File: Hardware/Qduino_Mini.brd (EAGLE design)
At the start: 20.3 x 38.1 mm, 40 parts, among them J1 LiPo, Q1 PFET, U1 ATMEGA32U41:1-LESS_PASTE, U2 MCP73831, U3 MAX17048, U4 AP2112K-3.3TRG-1, U5 MIGHTYQ-L-SILK, Y1 8MHZ

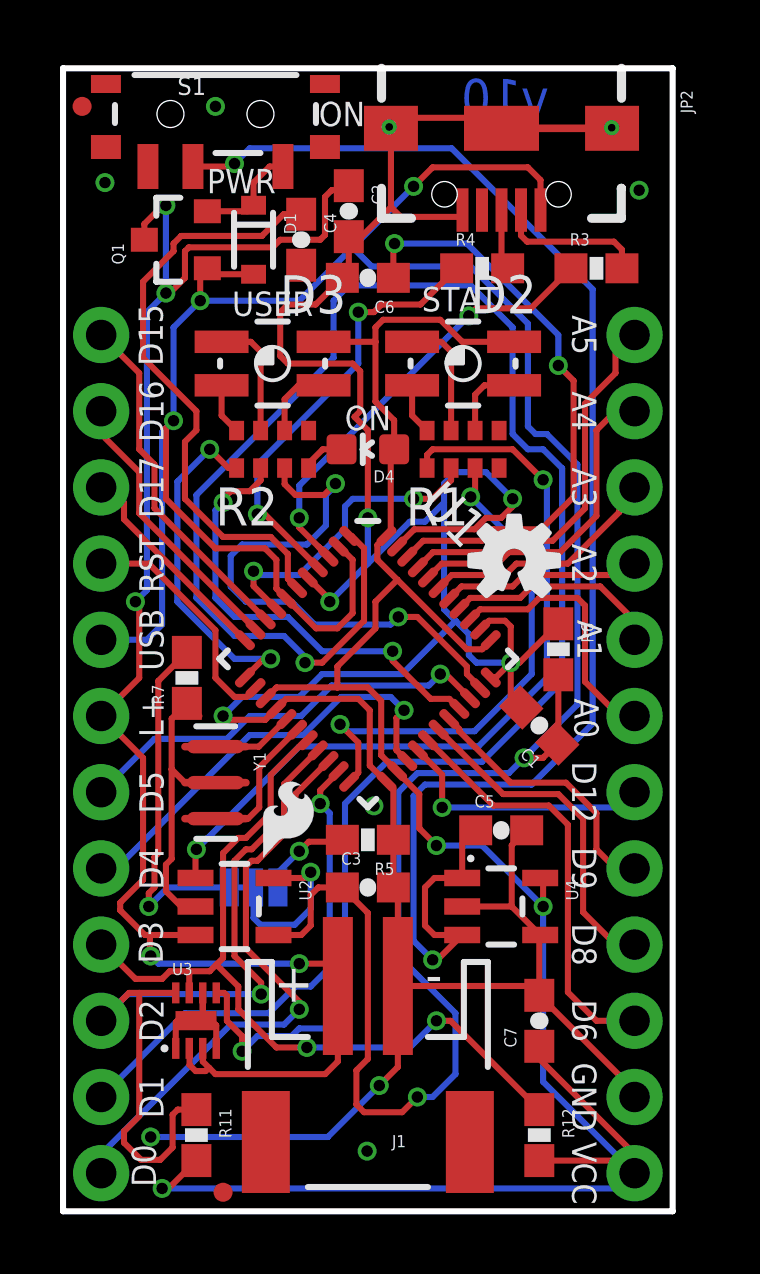
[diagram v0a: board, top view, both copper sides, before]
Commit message: Improved ground path from LiPo to GND pin nearby. Increased width of LiPo & Vbus by 25-50%
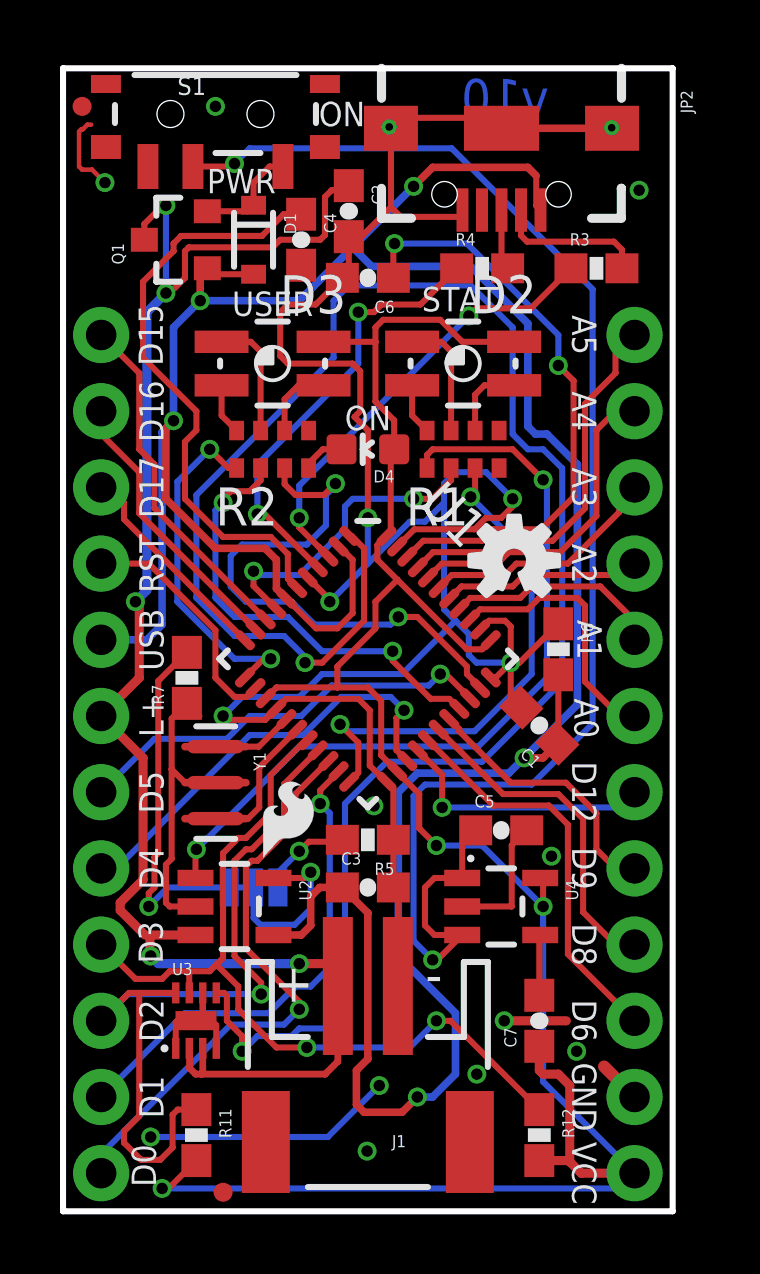
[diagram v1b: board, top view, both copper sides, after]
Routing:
- net GND: track 129.0 -> 121.5 mm, vias 12 -> 16
- net VCC: track 76.3 -> 75.3 mm
- net D6: track 14.0 -> 13.3 mm

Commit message: Fixed issues
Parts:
- Q1: value PFET -> ZXMP6A13FTA
- R1, R2: value 330 -> 1KΩ
- moved FID2 11.2 mm to (16.5, 0.71)
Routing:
- net GND: track 121.5 -> 114.3 mm, vias 16 -> 18
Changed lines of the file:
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@@
 <attribute name="VALUE" value="100k" x="16.51" y="18.7325" size="1.778" layer="27" rot="R270" display="off"/>
 </element>
-<element name="Q1" library="SparkFun-DiscreteSemi" package="SOT23-3" value="PFET" x="3.81" y="32.385" rot="R90">
+<element name="Q1" library="SparkFun-DiscreteSemi" package="SOT23-3" value="ZXMP6A13FTA" x="3.81" y="32.385" rot="R90">
 <attribute name="PROD_ID" value="TRANS-08285" x="3.81" y="32.385" size="1.778" layer="27" rot="R90" display="off"/>
 </element>
@@
 </element>
 <element name="D3" library="Testing" package="P-LCC-4-3" value="" x="6.985" y="28.2575" rot="R90">
-<attribute name="PROD_ID" value="DIO-12986" x="6.985" y="28.2575" size="1.778" layer="27" rot="R90" display="off"/>
-</element>
-<element name="R1" library="SparkFun-Passives" package="0603-ARV" value="330" x="13.335" y="25.4">
+<attribute name="PROD_ID" value="DIO-12985" x="6.985" y="28.2575" size="1.778" layer="27" rot="R90" display="off"/>
+</element>
+<element name="R1" library="SparkFun-Passives" package="0603-ARV" value="1KΩ" x="13.335" y="25.4">
 <attribute name="PROD_ID" value="RES-12985" x="13.335" y="25.4" size="1.778" layer="27" display="off"/>
 </element>
-<element name="R2" library="SparkFun-Passives" package="0603-ARV" value="330" x="6.985" y="25.4">
+<element name="R2" library="SparkFun-Passives" package="0603-ARV" value="1KΩ" x="6.985" y="25.4">
 <attribute name="PROD_ID" value="RES-12985" x="6.985" y="25.4" size="1.778" layer="27" display="off"/>
 </element>
@@
 <element name="LOGO3" library="SparkFun-Aesthetics" package="SFE_LOGO_FLAME_.1@1" value="SFE_LOGO_FLAME.1_INCH" x="6.35" y="11.43"/>
 <element name="FID1" library="SparkFun-Aesthetics" package="MICRO-FIDUCIAL" value="FIDUCIALUFIDUCIAL" x="0.635" y="36.83"/>
-<element name="FID2" library="SparkFun-Aesthetics" package="MICRO-FIDUCIAL" value="FIDUCIALUFIDUCIAL" x="5.334" y="0.635"/>
+<element name="FID2" library="SparkFun-Aesthetics" package="MICRO-FIDUCIAL" value="FIDUCIALUFIDUCIAL" x="16.51" y="0.7112"/>
 <element name="J1" library="SparkFun-Connectors" package="JST-2-SMD" value="LiPo" x="10.16" y="3.81" smashed="yes" rot="R180">
 <attribute name="PROD_ID" value="CONN-11443" x="10.16" y="3.81" size="1.778" layer="27" rot="R180" display="off"/>
@@
 <contactref element="JP2" pad="GND1"/>
 <contactref element="Y1" pad="2"/>
-<wire x1="14.615" y1="36.1" x2="18.3" y2="36.1" width="0.254" layer="1"/>
 <contactref element="JP3" pad="2"/>
-<wire x1="10.93" y1="36.1" x2="11.081" y2="36.1" width="0.2032" layer="1"/>
-<wire x1="11.081" y1="36.1" x2="11.43" y2="36.449" width="0.2032" layer="1"/>
-<wire x1="11.43" y1="36.449" x2="14.266" y2="36.449" width="0.2032" layer="1"/>
 <wire x1="14.266" y1="36.449" x2="14.615" y2="36.1" width="0.2032" layer="1"/>
 <contactref element="R2" pad="5"/>
@@
 <wire x1="0.635" y1="34.7218" x2="0.9652" y2="34.7218" width="0.1524" layer="1"/>
 <wire x1="0.9652" y1="34.7218" x2="1.397" y2="34.29" width="0.1524" layer="1"/>
+<via x="10.8712" y="36.1442" extent="1-16" drill="0.254"/>
+<via x="18.288" y="36.1188" extent="1-16" drill="0.254"/>
 </signal>
 <signal name="!RST">
@@
 <wire x1="11.635" y1="26.525" x2="12.135" y2="26.025" width="0.2032" layer="1"/>
 </signal>
-<signal name="N$9">
-<via x="10.8712" y="36.1442" extent="1-16" drill="0.254"/>
-</signal>
-<signal name="N$10">
-<via x="18.288" y="36.1188" extent="1-16" drill="0.254"/>
-</signal>
 </signals>

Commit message: Switched LEDs to those in the live library vs testing
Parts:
- D2, D3: device Testing:P-LCC-4-3 -> SparkFun-LED:P-LCC-4-3
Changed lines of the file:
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@@
 <?xml version="1.0" encoding="utf-8"?>
 <!DOCTYPE eagle SYSTEM "eagle.dtd">
-<eagle version="7.3.0">
+<eagle version="7.2.0">
 <drawing>
 <settings>
@@
 <element name="LOGO1" library="SparkFun-Aesthetics" package="OSHW-LOGO-S" value="OSHW-LOGOS" x="15.0368" y="21.6916"/>
 <element name="LOGO2" library="SparkFun-Aesthetics" package="SFE_LOGO_FLAME_.1" value="SFE_LOGO_FLAME.1_INCH" x="3.175" y="34.29" rot="MR0"/>
-<element name="D2" library="Testing" package="P-LCC-4-3" value="" x="13.335" y="28.2575" rot="R90">
+<element name="D2" library="SparkFun-LED" package="P-LCC-4-3" value="" x="13.335" y="28.2575" rot="R90">
 <attribute name="PROD_ID" value="DIO-12986" x="13.335" y="28.2575" size="1.778" layer="27" rot="R90" display="off"/>
 </element>
-<element name="D3" library="Testing" package="P-LCC-4-3" value="" x="6.985" y="28.2575" rot="R90">
-<attribute name="PROD_ID" value="DIO-12985" x="6.985" y="28.2575" size="1.778" layer="27" rot="R90" display="off"/>
+<element name="D3" library="SparkFun-LED" package="P-LCC-4-3" value="" x="6.985" y="28.2575" rot="R90">
+<attribute name="PROD_ID" value="DIO-12986" x="6.985" y="28.2575" size="1.778" layer="27" rot="R90" display="off"/>
 </element>
 <element name="R1" library="SparkFun-Passives" package="0603-ARV" value="1KΩ" x="13.335" y="25.4">

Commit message: Added 10KΩ pull-up to reset line
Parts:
- added R8: 10K, SparkFun-Resistors:0603-RES
- moved R7 0.18 mm to (3.95, 17.8), turned to 135 degrees
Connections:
- net !RST: now also R8.1
- net VCC: now also R8.2
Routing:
- net VCC: track 75.3 -> 79.6 mm

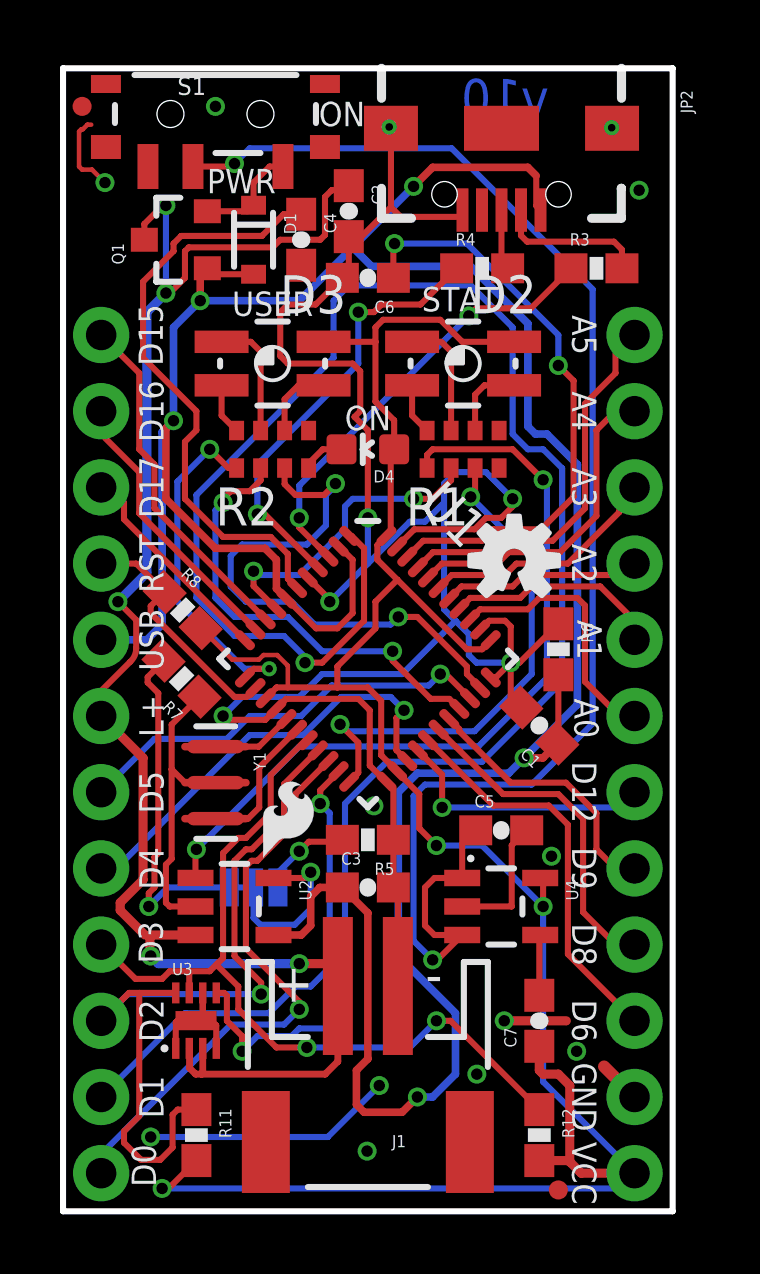
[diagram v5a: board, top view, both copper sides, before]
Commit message: Nudged traces and changed orientation of resistor
Nudged traces and moved 10K resistor for better trace continuity and
silk arrangement
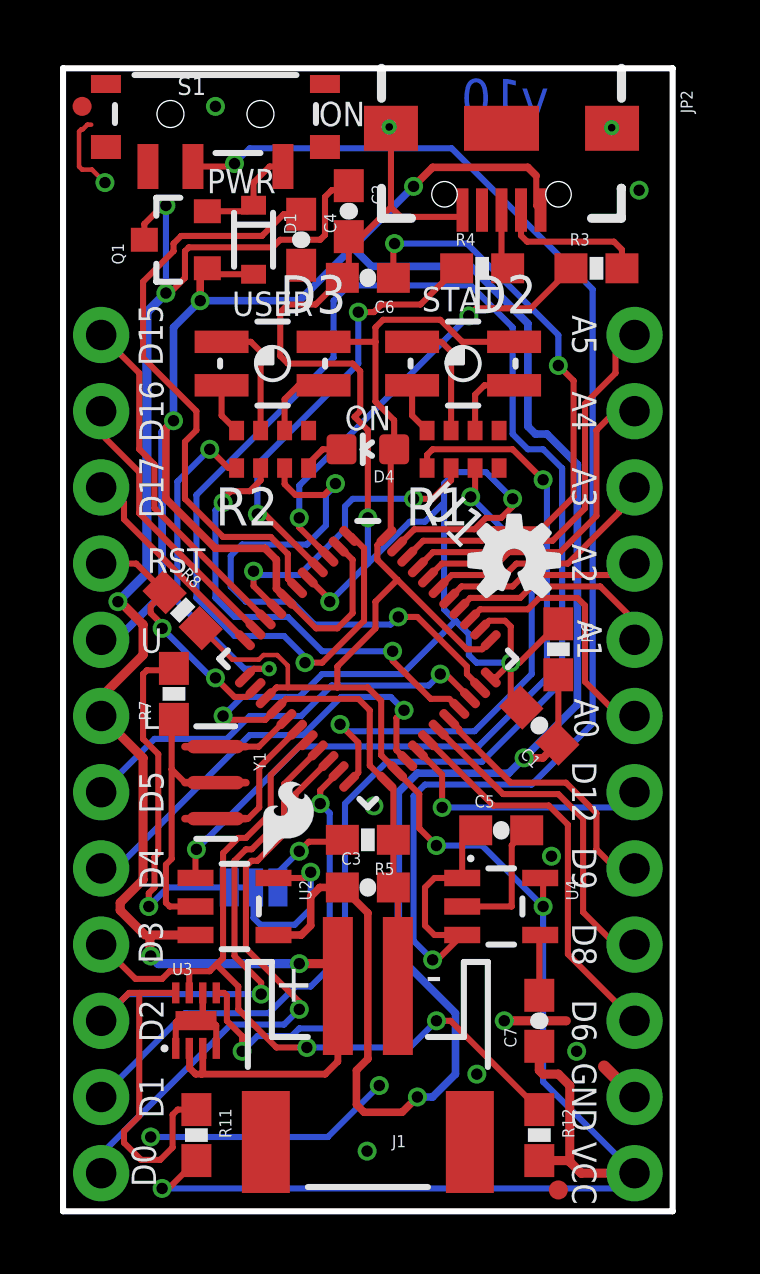
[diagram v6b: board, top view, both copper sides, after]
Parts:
- moved R7 0.57 mm to (3.70, 17.2), turned to 90 degrees
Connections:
- net LIPO renamed RS!T
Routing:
- net GND: track 114.1 -> 112.8 mm
- net VBUS: track 102.4 -> 101.8 mm
- net N$6: track 11.6 -> 12.1 mm
- net !RST: track 8.18 -> 8.25 mm, vias 0 -> 2
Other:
- board text added: "L"
- board text added: "U"
- board text removed: "L+"

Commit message: Cleaned up silk near recent changes
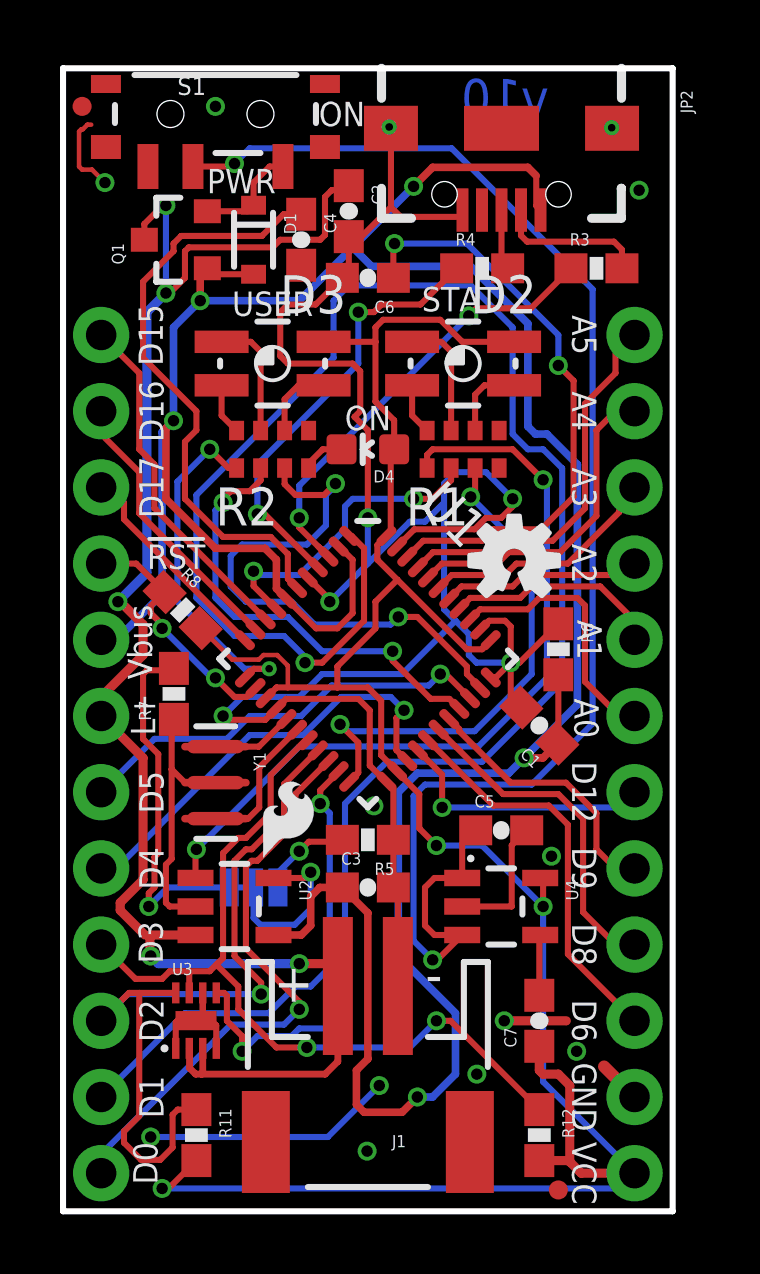
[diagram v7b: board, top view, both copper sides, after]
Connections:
- net RS!T renamed LIPO
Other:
- board text added: "!RST"
- board text added: "L+"
- board text added: "Vbus"
- board text removed: "L"
- board text removed: "RST"
- board text removed: "U"
